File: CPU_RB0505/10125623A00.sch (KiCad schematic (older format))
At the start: 0 parts

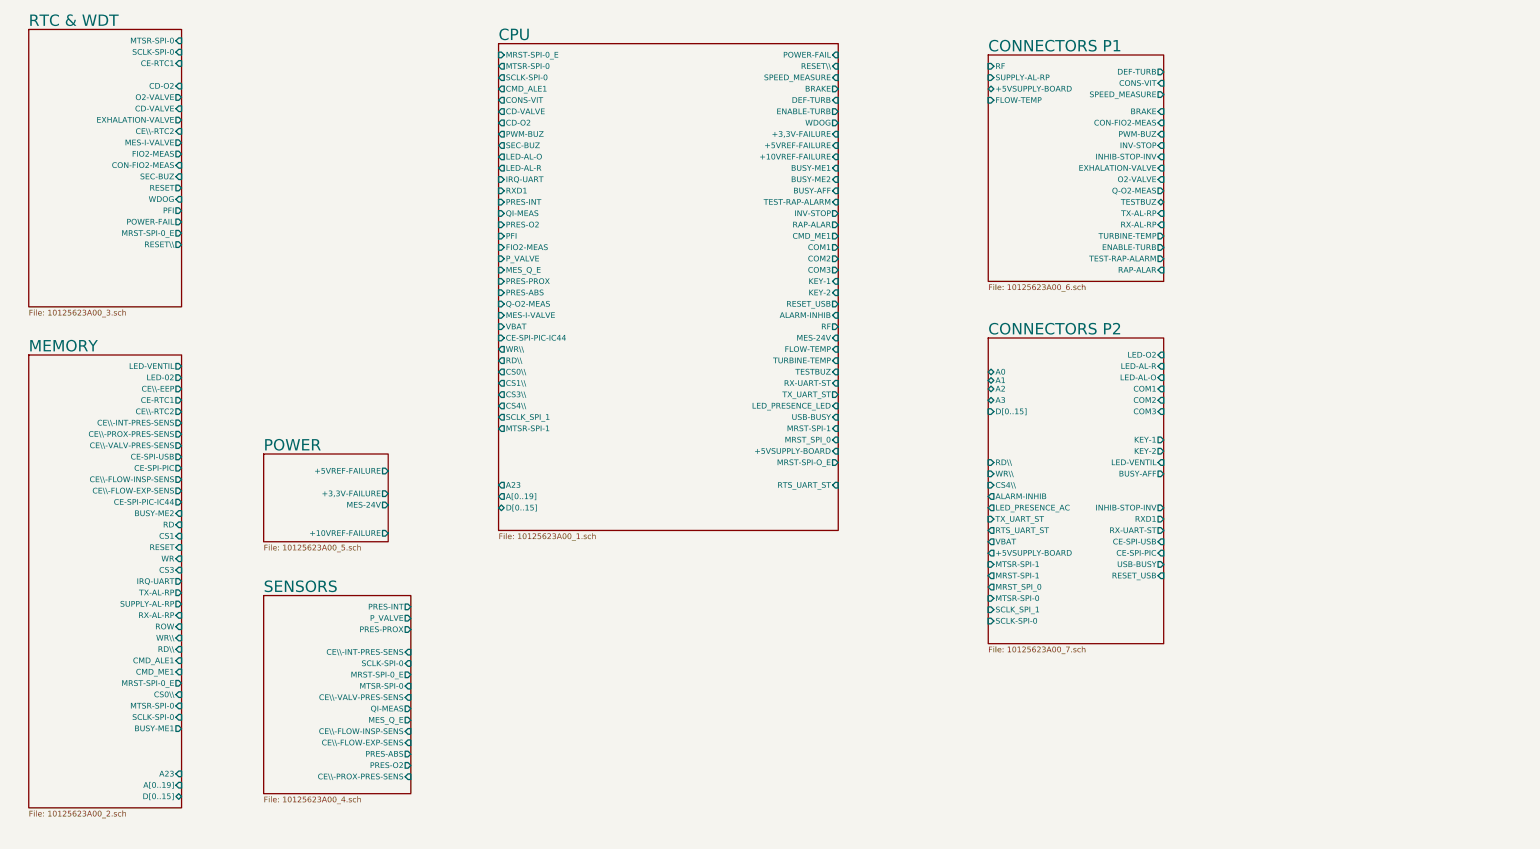
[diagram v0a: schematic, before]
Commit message: Sheet 1 corrections made: removed GLabels for power, some missed connections
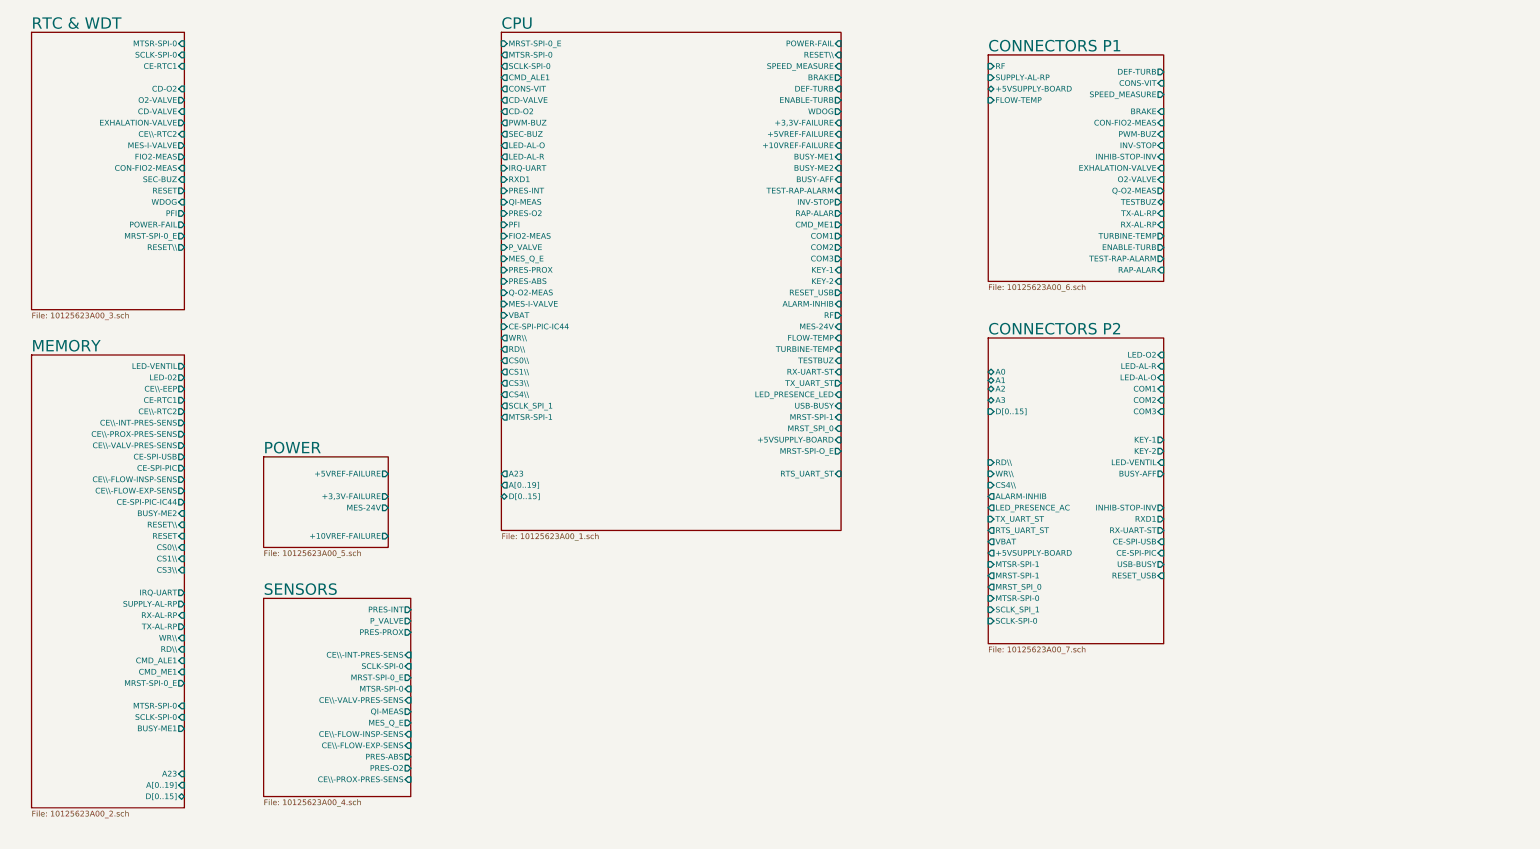
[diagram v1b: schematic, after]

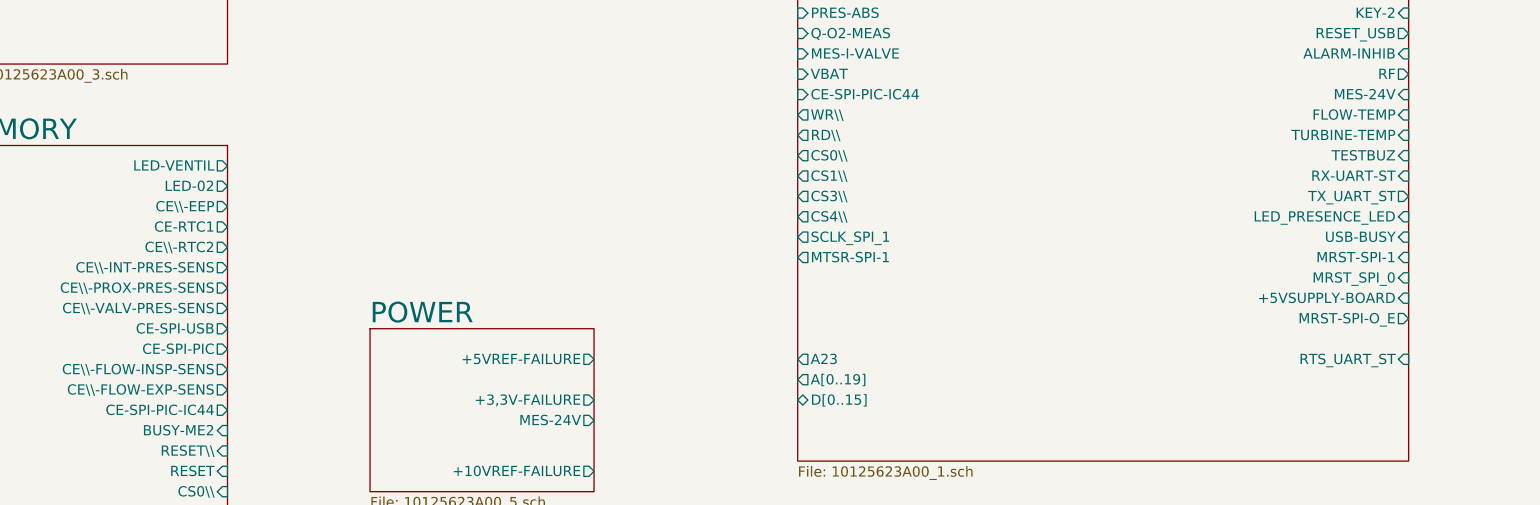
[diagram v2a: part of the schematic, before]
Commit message: Zero/Oh confusion: LED-02 => LED-O2, MRST-SPI-O_E => MRST-SPI-0_E
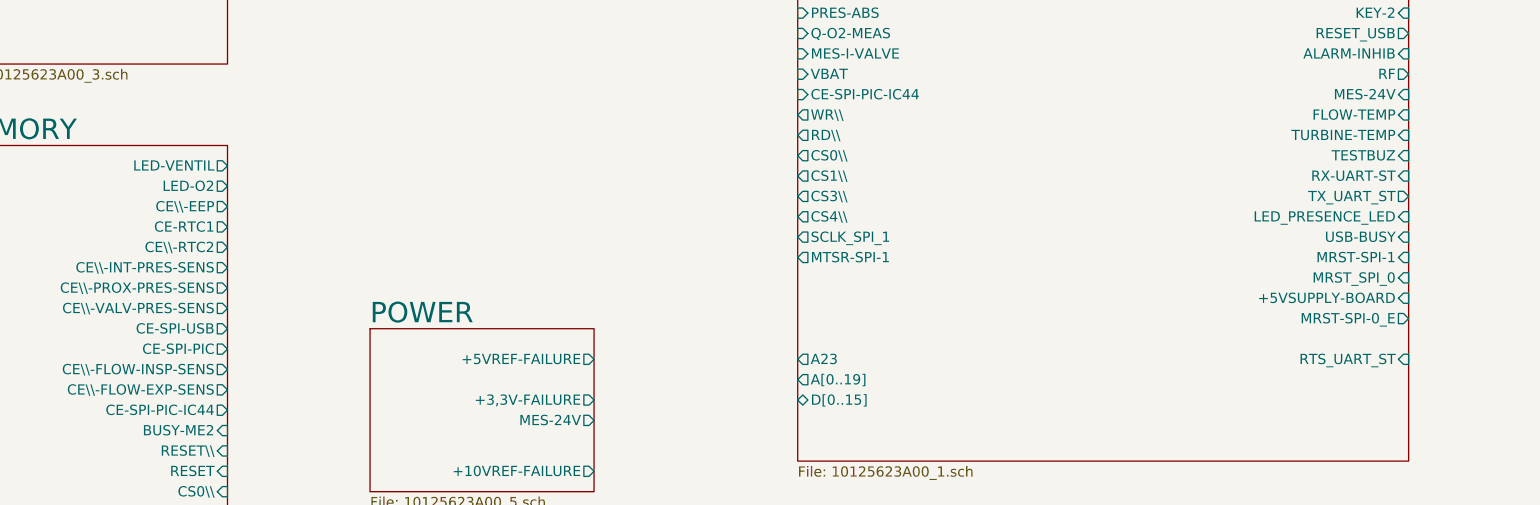
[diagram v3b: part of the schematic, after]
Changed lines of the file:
@@
 F72 "A23" O L 4950 4550 50
 F73 "A[0..19]" O L 4950 4650 50
-F74 "MRST-SPI-O_E" O R 7950 4350 50
+F74 "MRST-SPI-0_E" O R 7950 4350 50
 F75 "D[0..15]" B L 4950 4750 50
 F76 "RTS_UART_ST" I R 7950 4550 50
@@
 F1 "10125623A00_2.sch" 50
 F2 "LED-VENTIL" O R 2150 3600 50
-F3 "LED-02" O R 2150 3700 50
+F3 "LED-O2" O R 2150 3700 50
 F4 "CE\\-EEP" O R 2150 3800 50
 F5 "CE-RTC1" O R 2150 3900 50

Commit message: wip - organizing heir labels
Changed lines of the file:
@@
 F0 "CPU" 100
 F1 "10125623A00_1.sch" 50
-F2 "POWER-FAIL" I R 7950 750 50
-F3 "RESET\\" I R 7950 850 50
-F4 "SPEED_MEASURE" I R 7950 950 50
-F5 "BRAKE" O R 7950 1050 50
-F6 "DEF-TURB" I R 7950 1150 50
-F7 "ENABLE-TURB" O R 7950 1250 50
-F8 "WDOG" O R 7950 1350 50
-F9 "+3,3V-FAILURE" I R 7950 1450 50
-F10 "+5VREF-FAILURE" I R 7950 1550 50
-F11 "+10VREF-FAILURE" I R 7950 1650 50
-F12 "BUSY-ME1" I R 7950 1750 50
-F13 "BUSY-ME2" I R 7950 1850 50
-F14 "BUSY-AFF" I R 7950 1950 50
-F15 "TEST-RAP-ALARM" I R 7950 2050 50
-F16 "INV-STOP" O R 7950 2150 50
-F17 "RAP-ALAR" O R 7950 2250 50
-F18 "CMD_ME1" O R 7950 2350 50
-F19 "COM1" O R 7950 2450 50
-F20 "COM2" O R 7950 2550 50
-F21 "COM3" O R 7950 2650 50
-F22 "KEY-1" I R 7950 2750 50
-F23 "KEY-2" I R 7950 2850 50
-F24 "RESET_USB" O R 7950 2950 50
-F25 "ALARM-INHIB" I R 7950 3050 50
-F26 "RF" O R 7950 3150 50
-F27 "MRST-SPI-0_E" I L 4950 750 50
-F28 "MTSR-SPI-0" O L 4950 850 50
-F29 "SCLK-SPI-0" O L 4950 950 50
-F30 "CMD_ALE1" O L 4950 1050 50
-F31 "CONS-VIT" O L 4950 1150 50
-F32 "CD-VALVE" O L 4950 1250 50
-F33 "CD-O2" O L 4950 1350 50
-F34 "PWM-BUZ" O L 4950 1450 50
-F35 "SEC-BUZ" O L 4950 1550 50
-F36 "LED-AL-O" O L 4950 1650 50
-F37 "LED-AL-R" O L 4950 1750 50
+F2 "POWER-FAIL" I L 4950 700 50
+F3 "RESET\\" I L 4950 1100 50
+F4 "SPEED_MEASURE" I L 4950 1200 50
+F5 "BRAKE" O R 7950 1875 50
+F6 "DEF-TURB" I L 4950 1300 50
+F7 "ENABLE-TURB" O R 7950 1975 50
+F8 "WDOG" O R 7950 2075 50
+F9 "+3,3V-FAILURE" I L 4950 800 50
+F10 "+5VREF-FAILURE" I L 4950 900 50
+F11 "+10VREF-FAILURE" I L 4950 1000 50
+F12 "BUSY-ME1" I L 4950 1550 50
+F13 "BUSY-ME2" I L 4950 1650 50
+F14 "BUSY-AFF" I L 4950 1750 50
+F15 "TEST-RAP-ALARM" I L 4950 3375 50
+F16 "INV-STOP" O R 7950 2875 50
+F17 "RAP-ALAR" O R 7950 2975 50
+F18 "CMD_ME1" O R 7950 3075 50
+F19 "COM1" O R 7950 3175 50
+F20 "COM2" O R 7950 3275 50
+F21 "COM3" O R 7950 3375 50
+F22 "KEY-1" I L 4950 3475 50
+F23 "KEY-2" I L 4950 3575 50
+F24 "RESET_USB" O R 7950 1050 50
+F25 "ALARM-INHIB" I L 4950 3675 50
+F26 "RF" O R 7950 3575 50
+F27 "MRST-SPI-0_E" I L 4950 4900 50
+F28 "MTSR-SPI-0" O R 7950 4900 50
+F29 "SCLK-SPI-0" O R 7950 4975 50
+F30 "CMD_ALE1" O R 7950 1775 50
+F31 "CONS-VIT" O R 7950 2175 50
+F32 "CD-VALVE" O R 7950 2275 50
+F33 "CD-O2" O R 7950 2375 50
+F34 "PWM-BUZ" O R 7950 2475 50
+F35 "SEC-BUZ" O R 7950 2575 50
+F36 "LED-AL-O" O R 7950 2675 50
+F37 "LED-AL-R" O R 7950 2775 50
 F38 "IRQ-UART" I L 4950 1850 50
 F39 "RXD1" I L 4950 1950 50
@@
 F50 "MES-I-VALVE" I L 4950 3050 50
 F51 "VBAT" I L 4950 3150 50
-F52 "MES-24V" I R 7950 3250 50
-F53 "FLOW-TEMP" I R 7950 3350 50
-F54 "TURBINE-TEMP" I R 7950 3450 50
-F55 "TESTBUZ" I R 7950 3550 50
-F56 "RX-UART-ST" I R 7950 3650 50
-F57 "TX_UART_ST" O R 7950 3750 50
-F58 "LED_PRESENCE_LED" I R 7950 3850 50
-F59 "USB-BUSY" I R 7950 3950 50
-F60 "MRST-SPI-1" I R 7950 4050 50
-F61 "MRST_SPI_0" I R 7950 4150 50
-F62 "+5VSUPPLY-BOARD" I R 7950 4250 50
-F63 "CE-SPI-PIC-IC44" I L 4950 3250 50
-F64 "RD\\" O L 4950 3450 50
-F65 "WR\\" O L 4950 3350 50
-F66 "CS0\\" O L 4950 3550 50
-F67 "CS1\\" O L 4950 3650 50
-F68 "CS3\\" O L 4950 3750 50
-F69 "CS4\\" O L 4950 3850 50
-F70 "SCLK_SPI_1" O L 4950 3950 50
-F71 "MTSR-SPI-1" O L 4950 4050 50
-F72 "A23" O L 4950 4550 50
-F73 "A[0..19]" O L 4950 4650 50
-F74 "MRST-SPI-0_E" O R 7950 4350 50
-F75 "D[0..15]" B L 4950 4750 50
-F76 "RTS_UART_ST" I R 7950 4550 50
+F52 "MES-24V" I L 4950 3775 50
+F53 "FLOW-TEMP" I L 4950 3875 50
+F54 "TURBINE-TEMP" I L 4950 4000 50
+F55 "TESTBUZ" I L 4950 4100 50
+F56 "RX-UART-ST" I L 4950 4200 50
+F57 "TX_UART_ST" O R 7950 4200 50
+F58 "LED_PRESENCE_LED" I L 4950 4300 50
+F59 "USB-BUSY" I L 4950 4400 50
+F60 "MRST-SPI-1" I L 4950 4800 50
+F61 "MRST_SPI_0" I L 4950 4700 50
+F62 "+5VSUPPLY-BOARD" I L 4950 4500 50
+F63 "CE-SPI-PIC-IC44" I L 4950 4950 50
+F64 "RD\\" O R 7950 3800 50
+F65 "WR\\" O R 7950 3725 50
+F66 "CS0\\" O R 7950 3875 50
+F67 "CS1\\" O R 7950 3950 50
+F68 "CS3\\" O R 7950 4025 50
+F69 "CS4\\" O R 7950 4100 50
+F70 "SCLK_SPI_1" O R 7950 4275 50
+F71 "MTSR-SPI-1" O R 7950 4350 50
+F72 "A23" O R 7950 925 50
+F73 "A[0..19]" O R 7950 825 50
+F74 "MRST-SPI-0_E" O R 7950 4825 50
+F75 "D[0..15]" B R 7950 725 50
+F76 "RTS_UART_ST" I L 4950 4600 50
 $EndSheet
 $Sheet
@@
 F38 "D[0..15]" I L 9250 4000 50
 $EndSheet
+Text Label 4950 1100 2    50   ~ 0
+RESET\
 $EndSCHEMATC

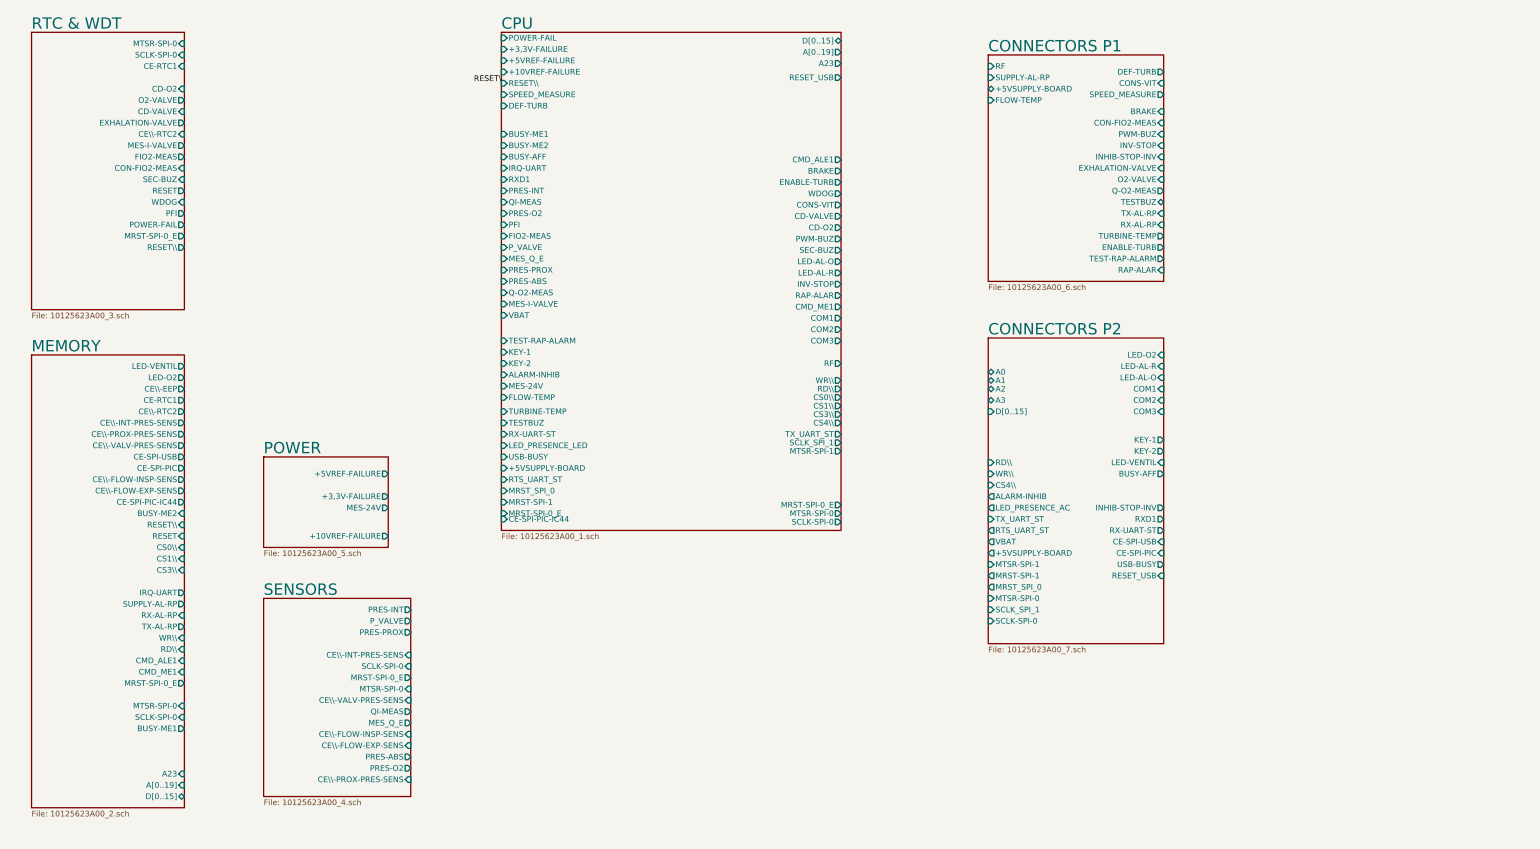
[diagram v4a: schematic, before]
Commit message: Organized heir labels
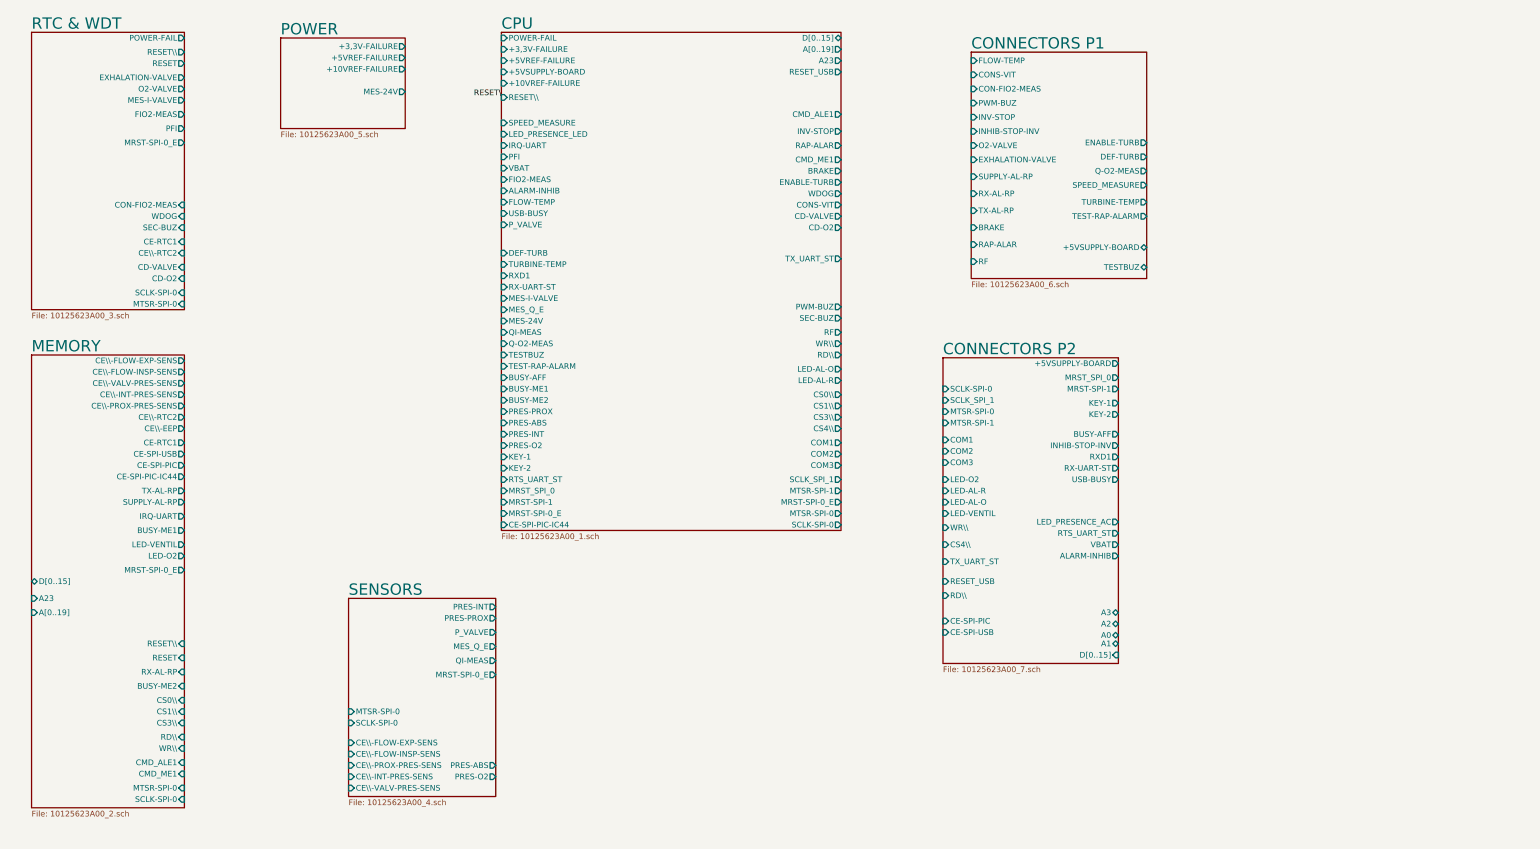
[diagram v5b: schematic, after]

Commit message: Placed net labels
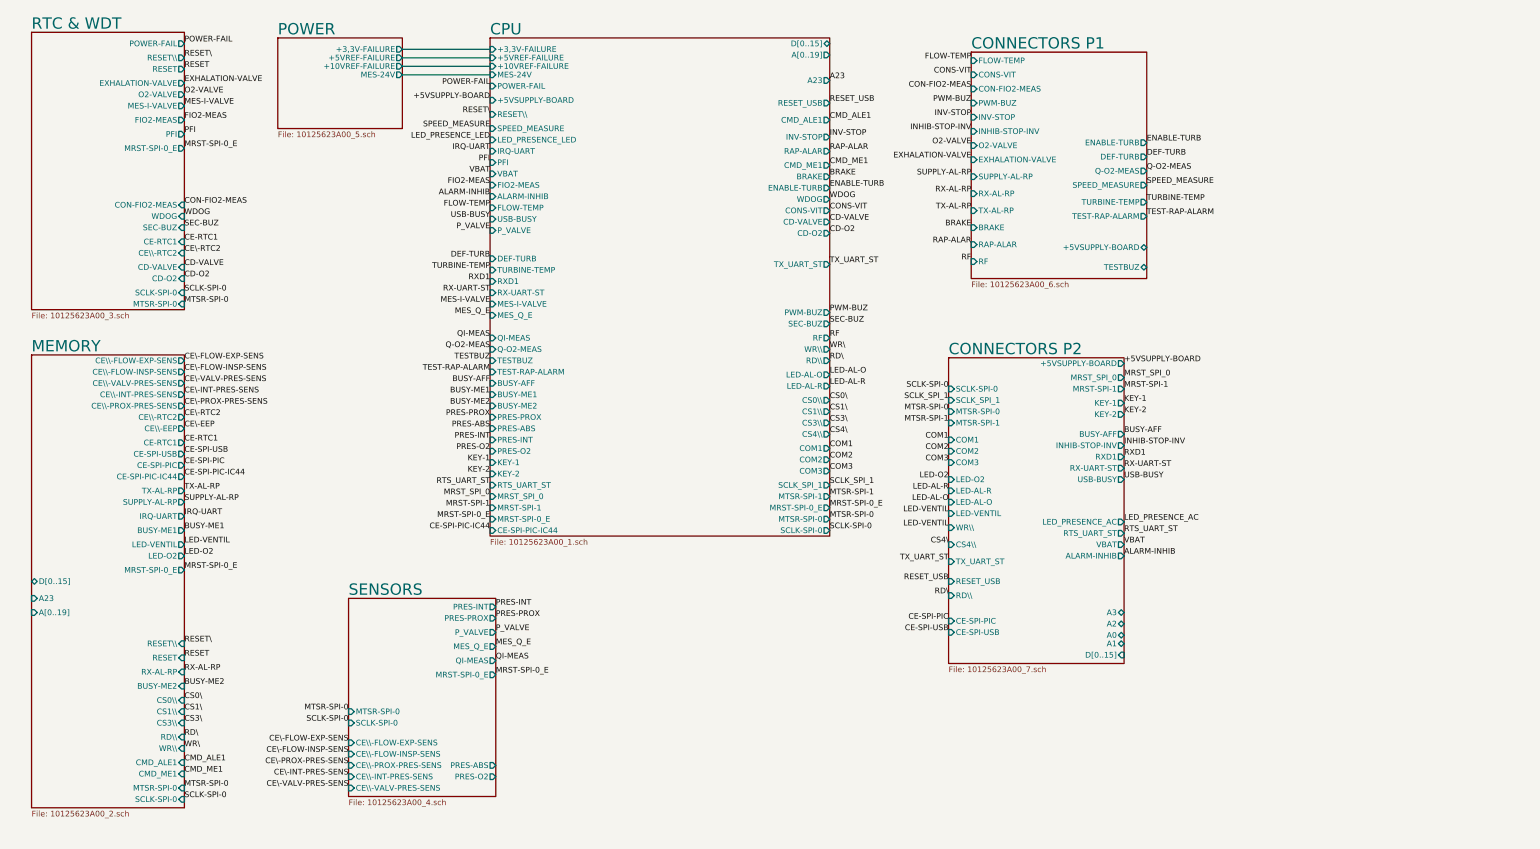
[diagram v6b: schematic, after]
